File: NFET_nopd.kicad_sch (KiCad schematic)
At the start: 1 part, among them Q4 BSS138LT3G

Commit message: modified
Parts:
- renumbered Q4 to Q5
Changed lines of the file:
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@@
     (effects (font (size 1.27 1.27)) (justify right))
   )
-  (symbol (lib_id "Device:Q_NMOS_GSD") (at 156.21 87.63 0)
+  (symbol (lib_id "Device:Q_NMOS_GSD") (at 156.21 87.63 0) (unit 1)
     (in_bom yes) (on_board yes)
-    (property "Reference" "Q4" (id 0) (at 161.417 86.4616 0)
+    (property "Reference" "Q5" (id 0) (at 161.417 86.4616 0)
       (effects (font (size 1.27 1.27)) (justify left))
     )

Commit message: 24V updates
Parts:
- renumbered Q5 to Q3
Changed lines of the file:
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@@
   (symbol (lib_id "Device:Q_NMOS_GSD") (at 156.21 87.63 0) (unit 1)
     (in_bom yes) (on_board yes)
-    (property "Reference" "Q5" (id 0) (at 161.417 86.4616 0)
+    (property "Reference" "Q3" (id 0) (at 161.417 86.4616 0)
       (effects (font (size 1.27 1.27)) (justify left))
     )

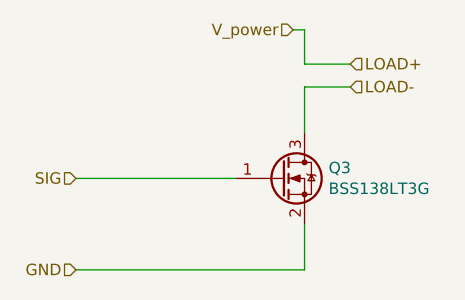
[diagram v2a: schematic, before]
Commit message: fix LT1161 symbol/sch
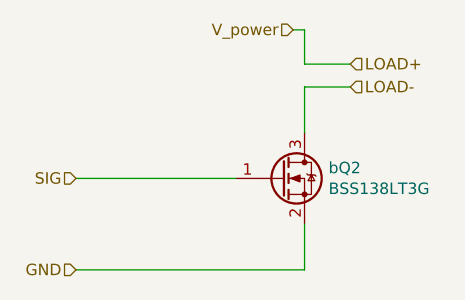
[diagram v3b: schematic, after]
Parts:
- renumbered Q3 to bQ2
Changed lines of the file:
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@@
   (symbol (lib_id "Device:Q_NMOS_GSD") (at 156.21 87.63 0) (unit 1)
     (in_bom yes) (on_board yes)
-    (property "Reference" "Q3" (id 0) (at 161.417 86.4616 0)
+    (property "Reference" "bQ2" (id 0) (at 161.417 86.4616 0)
       (effects (font (size 1.27 1.27)) (justify left))
     )
